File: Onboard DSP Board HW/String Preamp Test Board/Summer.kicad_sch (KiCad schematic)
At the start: 16 parts, among them U2 TLV9001IDCK

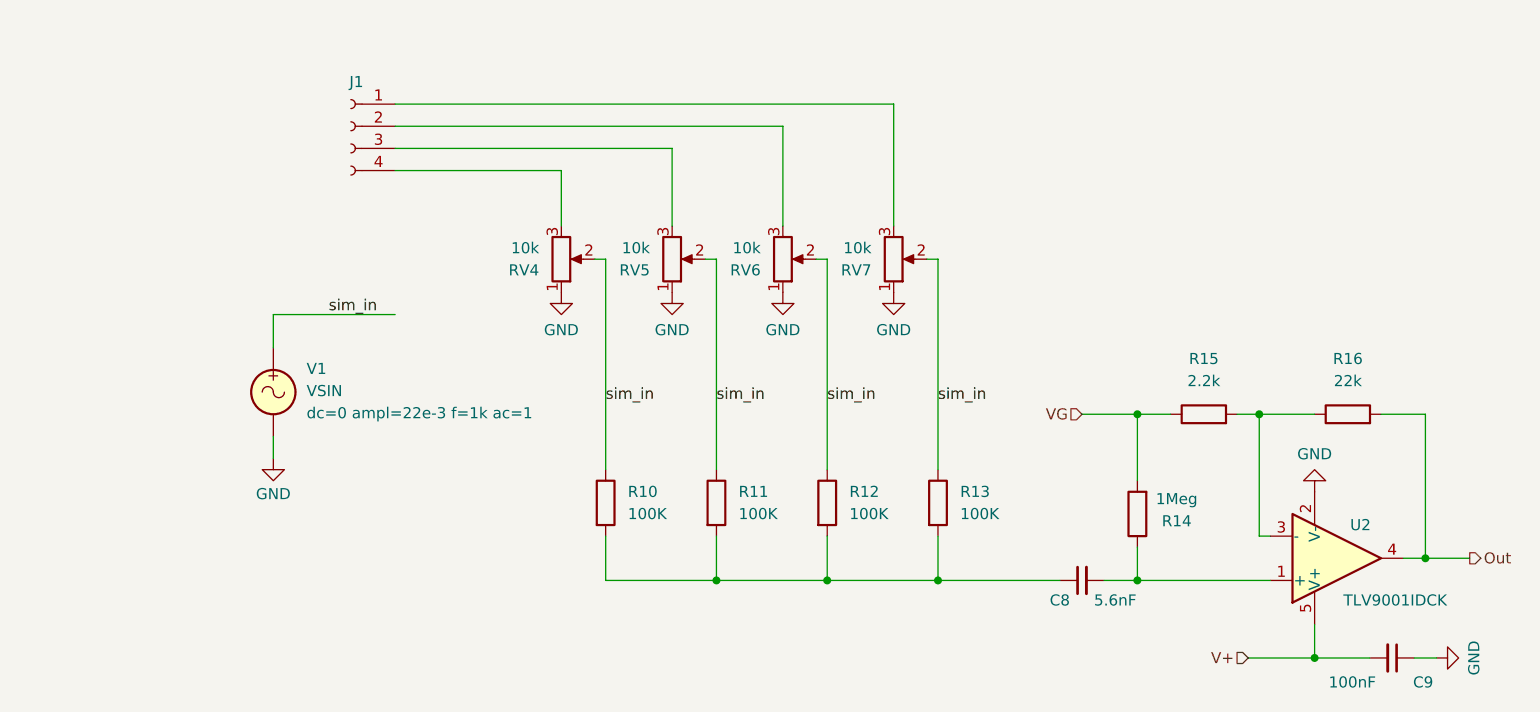
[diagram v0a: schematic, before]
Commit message: move bias to cavity
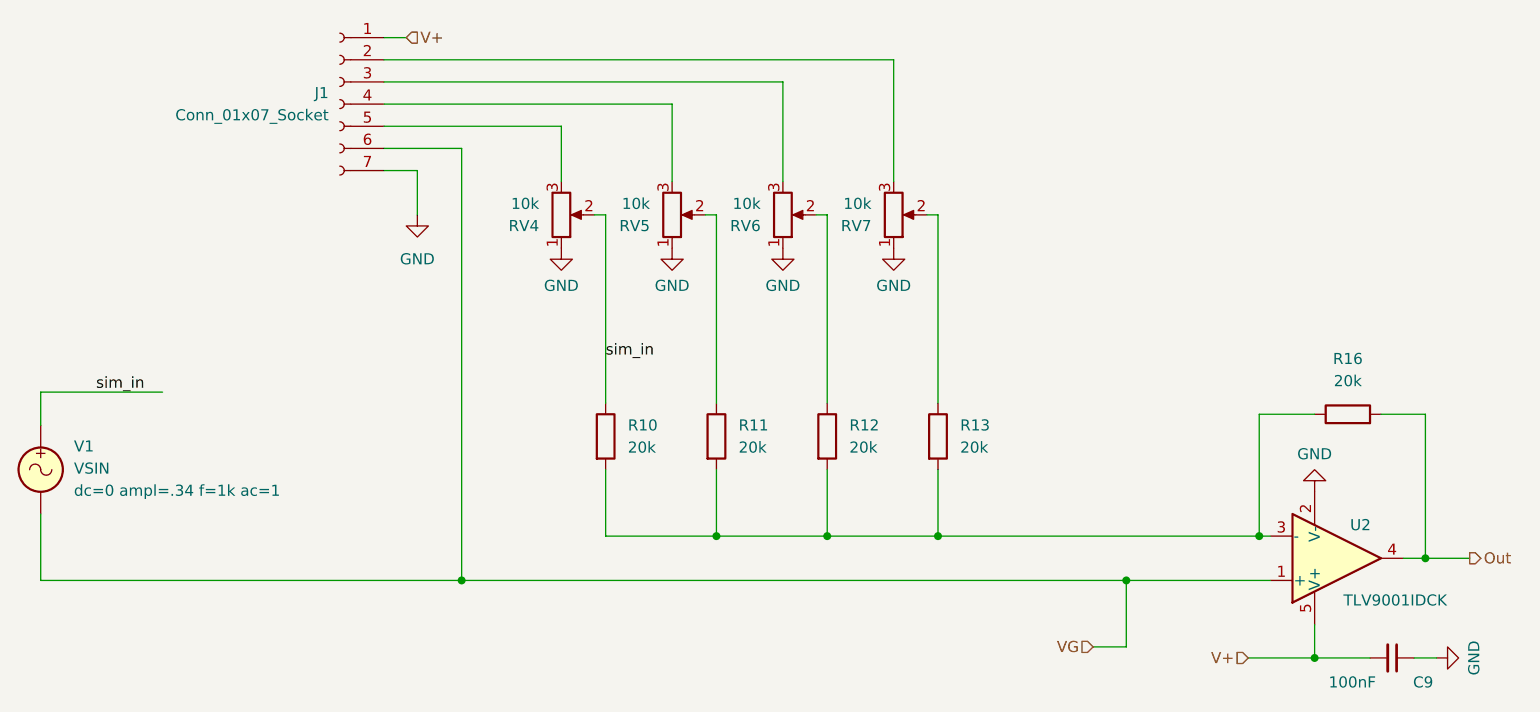
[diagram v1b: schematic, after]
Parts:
- removed C8: 5.6nF, Capacitor_SMD:C_0402_1005Metric, symbol Device:C_Small
- removed J1: (no value), Connector_PinHeader_2.00mm:PinHeader_1x04_P2.00mm_Vertical, symbol Connector:Conn_01x04_Socket
- removed R14: 1Meg, Resistor_SMD:R_0402_1005Metric, symbol Device:R
- removed R15: 2.2k, Resistor_SMD:R_0402_1005Metric, symbol Device:R
- added J1: Conn_01x07_Socket, symbol Connector:Conn_01x07_Socket
- R10, R11, R12, R13: value 100K -> 20k
- R16: value 22k -> 20k
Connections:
- net GND: now also J1.7 (Pin_7); no longer V1.2
- net V+: now also J1.1 (Pin_1)
- net VG: now also U2.1 (+), V1.2, J1.6 (Pin_6)
- net sim_in: no longer R11.1, R12.1, R13.1, RV5.2, RV6.2, RV7.2
- net at R10.2, R11.2, R12.2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: now also R16.1, U2.3 (-)
- net at RV5.3: now also J1.4 (Pin_4)
- net at RV6.3: now also J1.3 (Pin_3)
- net at RV7.3: now also J1.2 (Pin_2)
- net at RV4.3: now also J1.5 (Pin_5)
- new net: R11.1, RV5.2
- new net: R12.1, RV6.2
- new net: R13.1, RV7.2
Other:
- moved on the sheet: R10, R11, R12, R13, RV4, RV5, RV6, RV7, V1
